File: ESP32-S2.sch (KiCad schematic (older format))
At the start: 4 parts, among them J2 Conn_01x06, U2 esp32-s2-wroom

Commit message: First layouting
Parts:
- U2: symbol ESP32-S2:esp32-s2-wroom -> ESP32_Tasmota_Fan-rescue:esp32-s2-wroom-ESP32-S2
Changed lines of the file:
@@
 $EndDescr
 $Comp
-L ESP32-S2:esp32-s2-wroom U2
+L ESP32_Tasmota_Fan-rescue:esp32-s2-wroom-ESP32-S2 U2
 U 1 1 618CEA8A
 P 5700 3400

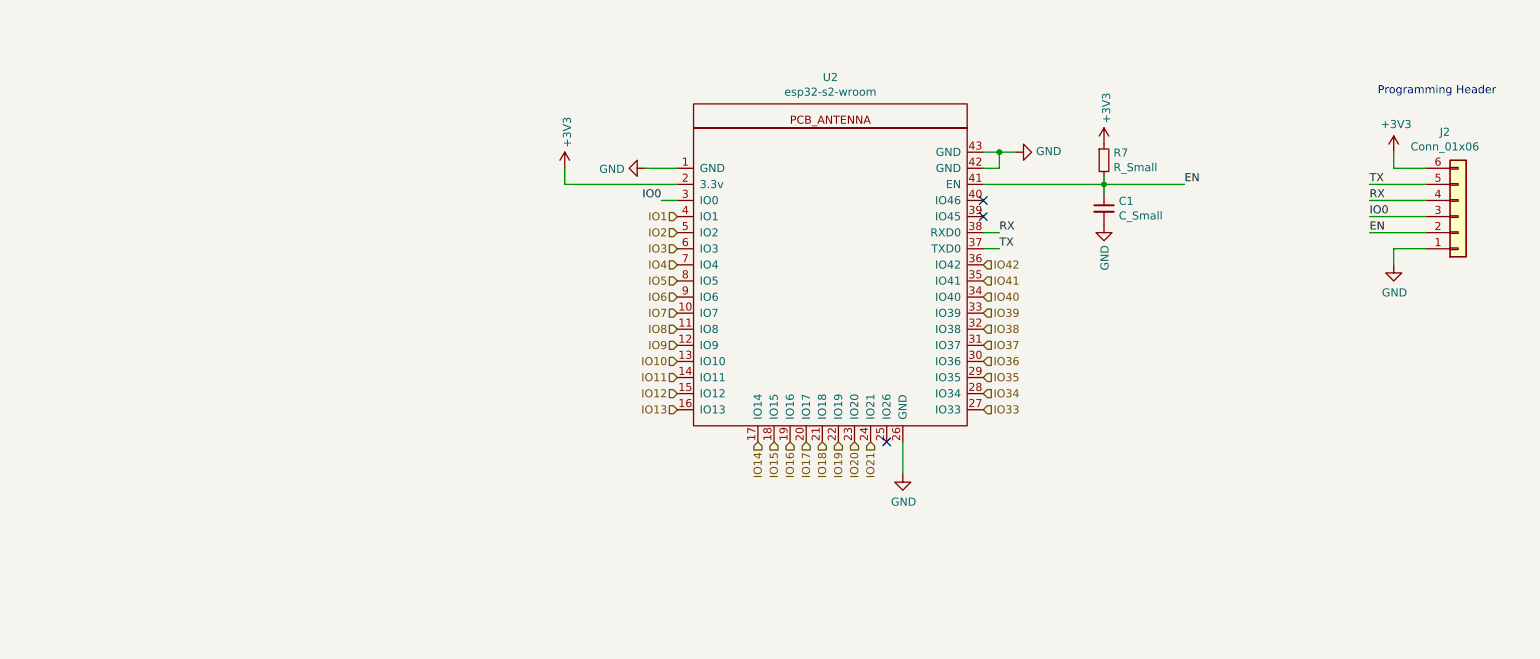
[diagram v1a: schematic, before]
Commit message: First iteration with new ES32 - but not S2
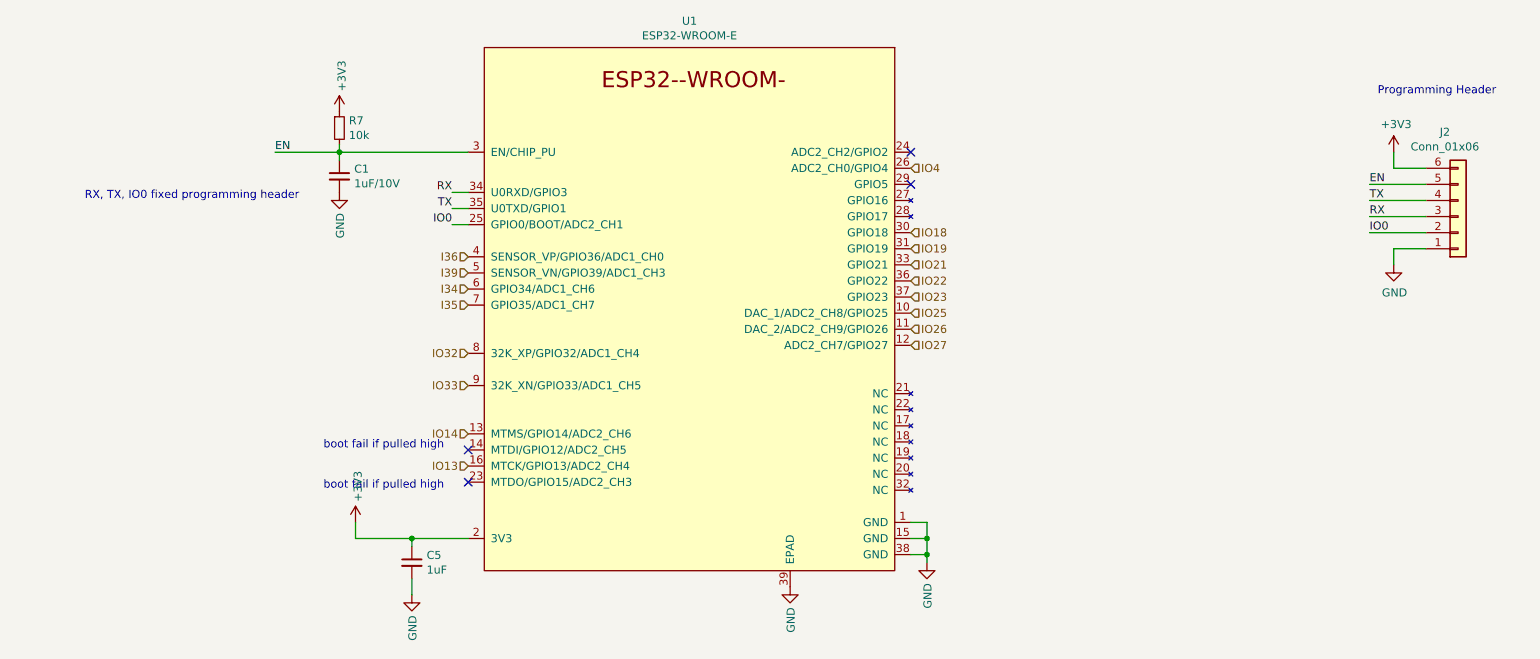
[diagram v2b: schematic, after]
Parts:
- removed U2: esp32-s2-wroom, ESP32-S2:esp32-s2-wrooom, symbol ESP32_Tasmota_Fan-rescue:esp32-s2-wroom-ESP32-S2
- added C5: 1uF, Capacitor_SMD:C_0805_2012Metric, symbol Device:C_Small
- added U1: ESP32-WROOM-E, espressif:ESP32-WROOM-32E, symbol Espressif:ESP32-WROOM-E
- C1: value C_Small -> 1uF/10V; LCSC (none) -> C1779
- R7: value R_Small -> 10k; LCSC (none) -> C17414
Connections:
- net +3V3: now also C5.1, U1.2 (3V3)
- net EN: now also J2.5 (Pin_5), U1.3 (EN/CHIP_PU); no longer J2.2 (Pin_2)
- net GND: now also C5.2, U1.1 (GND), U1.15 (GND), U1.38 (GND), U1.39 (EPAD)
- net IO0: now also J2.2 (Pin_2), U1.25 (GPIO0/BOOT/ADC2_CH1); no longer J2.3 (Pin_3)
- net IO13: now also U1.16 (MTCK/GPIO13/ADC2_CH4)
- net IO14: now also U1.13 (MTMS/GPIO14/ADC2_CH6)
- net IO18: now also U1.30 (GPIO18)
- net IO19: now also U1.31 (GPIO19)
- net IO21: now also U1.33 (GPIO21)
- net IO33: now also U1.9 (32K_XN/GPIO33/ADC1_CH5)
- net IO4: now also U1.26 (ADC2_CH0/GPIO4)
- net RX: now also J2.3 (Pin_3), U1.34 (U0RXD/GPIO3); no longer J2.4 (Pin_4)
- net TX: now also J2.4 (Pin_4), U1.35 (U0TXD/GPIO1); no longer J2.5 (Pin_5)
- new net I34: U1.6 (GPIO34/ADC1_CH6)
- new net I35: U1.7 (GPIO35/ADC1_CH7)
- new net I36: U1.4 (SENSOR_VP/GPIO36/ADC1_CH0)
- new net I39: U1.5 (SENSOR_VN/GPIO39/ADC1_CH3)
- new net IO22: U1.36 (GPIO22)
- new net IO23: U1.37 (GPIO23)
- new net IO25: U1.10 (DAC_1/ADC2_CH8/GPIO25)
- new net IO26: U1.11 (DAC_2/ADC2_CH9/GPIO26)
- new net IO27: U1.12 (ADC2_CH7/GPIO27)
- new net IO32: U1.8 (32K_XP/GPIO32/ADC1_CH4)
- no-connect marks 3 -> 4
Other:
- note added: "RX, TX, IO0 fixed programming header"
- note added: "boot fail if pulled high"
- moved on the sheet: C1, R7

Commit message: Version open for review
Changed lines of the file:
@@
 L power:+3V3 #PWR037
 U 1 1 618D1013
-P 2700 4950
-F 0 "#PWR037" H 2700 4800 50  0001 C CNN
-F 1 "+3V3" V 2715 5078 50  0000 L CNN
-F 2 "" H 2700 4950 50  0001 C CNN
-F 3 "" H 2700 4950 50  0001 C CNN
-	1    2700 4950
+P 2200 4950
+F 0 "#PWR037" H 2200 4800 50  0001 C CNN
+F 1 "+3V3" V 2215 5078 50  0000 L CNN
+F 2 "" H 2200 4950 50  0001 C CNN
+F 3 "" H 2200 4950 50  0001 C CNN
+	1    2200 4950
 	1    0    0    -1
 $EndComp
@@
 	3400 5050 3050 5050
 Wire Wire Line
-	2700 5050 2700 4950
+	2200 5050 2200 4950
 Text Label 2200 2650 0    50   ~ 0
 EN
 Text HLabel 6150 2750 2    50   Input ~ 0
 IO4
-Text HLabel 6150 3550 2    50   Input ~ 0
+Text HLabel 6250 3550 2    50   Input ~ 0
 IO23
-Text HLabel 6150 3850 2    50   Input ~ 0
+Text HLabel 6250 3850 2    50   Input ~ 0
 IO27
-Text HLabel 6150 3750 2    50   Input ~ 0
+Text HLabel 6250 3750 2    50   Input ~ 0
 IO26
-Text HLabel 6150 3650 2    50   Input ~ 0
+Text HLabel 6250 3650 2    50   Input ~ 0
 IO25
-Text HLabel 6150 3150 2    50   Input ~ 0
+Text HLabel 6250 3150 2    50   Input ~ 0
 IO18
-Text HLabel 6150 3250 2    50   Input ~ 0
+Text HLabel 6250 3250 2    50   Input ~ 0
 IO19
-Text HLabel 6150 3450 2    50   Input ~ 0
+Text HLabel 6250 3450 2    50   Input ~ 0
 IO22
-Text HLabel 6150 3350 2    50   Input ~ 0
+Text HLabel 6250 3350 2    50   Input ~ 0
 IO21
-Text HLabel 3400 3300 0    50   Input ~ 0
+Text HLabel 3300 3300 0    50   Input ~ 0
 I36
-Text HLabel 3400 3400 0    50   Input ~ 0
+Text HLabel 3300 3400 0    50   Input ~ 0
 I39
-Text HLabel 3400 3500 0    50   Input ~ 0
+Text HLabel 3300 3500 0    50   Input ~ 0
 I34
-Text HLabel 3400 3600 0    50   Input ~ 0
+Text HLabel 3300 3600 0    50   Input ~ 0
 I35
 Text HLabel 3400 3900 0    50   Input ~ 0
@@
 Wire Wire Line
 	3050 5100 3050 5050
+Wire Wire Line
+	6150 3550 6250 3550
+Wire Wire Line
+	6150 3150 6250 3150
+Wire Wire Line
+	6150 3250 6250 3250
+Wire Wire Line
+	6150 3350 6250 3350
+Wire Wire Line
+	6150 3450 6250 3450
+Wire Wire Line
+	6150 3650 6250 3650
+Wire Wire Line
+	6150 3750 6250 3750
+Wire Wire Line
+	6150 3850 6250 3850
+Wire Wire Line
+	3300 3300 3400 3300
+Wire Wire Line
+	3300 3400 3400 3400
+Wire Wire Line
+	3300 3500 3400 3500
+Wire Wire Line
+	3300 3600 3400 3600
+Wire Wire Line
+	2200 5050 3050 5050
 Connection ~ 3050 5050
-Wire Wire Line
-	3050 5050 2700 5050
 $EndSCHEMATC
